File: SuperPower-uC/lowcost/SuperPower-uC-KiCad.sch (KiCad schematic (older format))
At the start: 0 parts

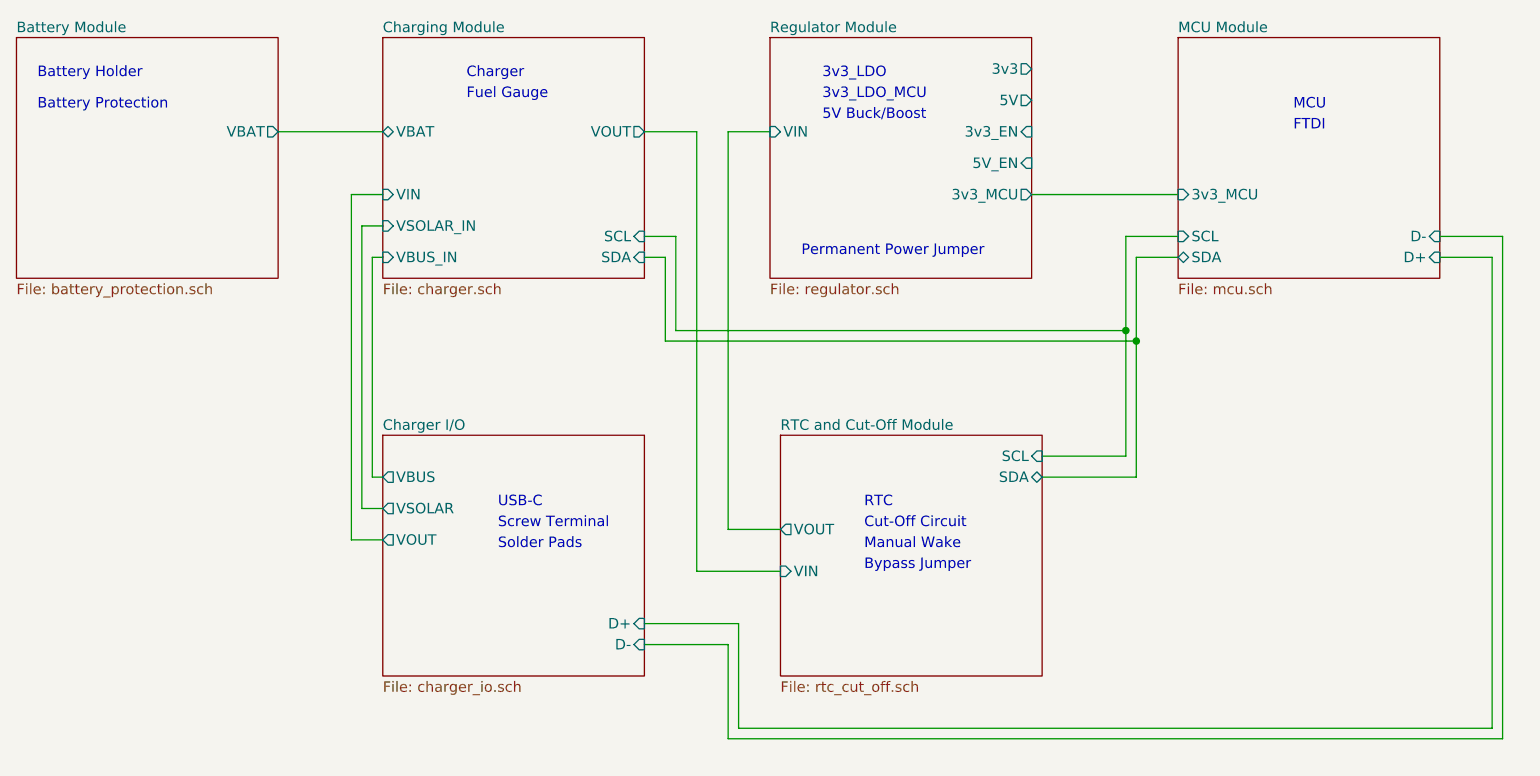
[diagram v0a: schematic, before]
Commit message: int pins and charging module
added Interrupt pins to the main sheet and finished the charging module sub sheet (with charger, fuel Gauge and power on int)
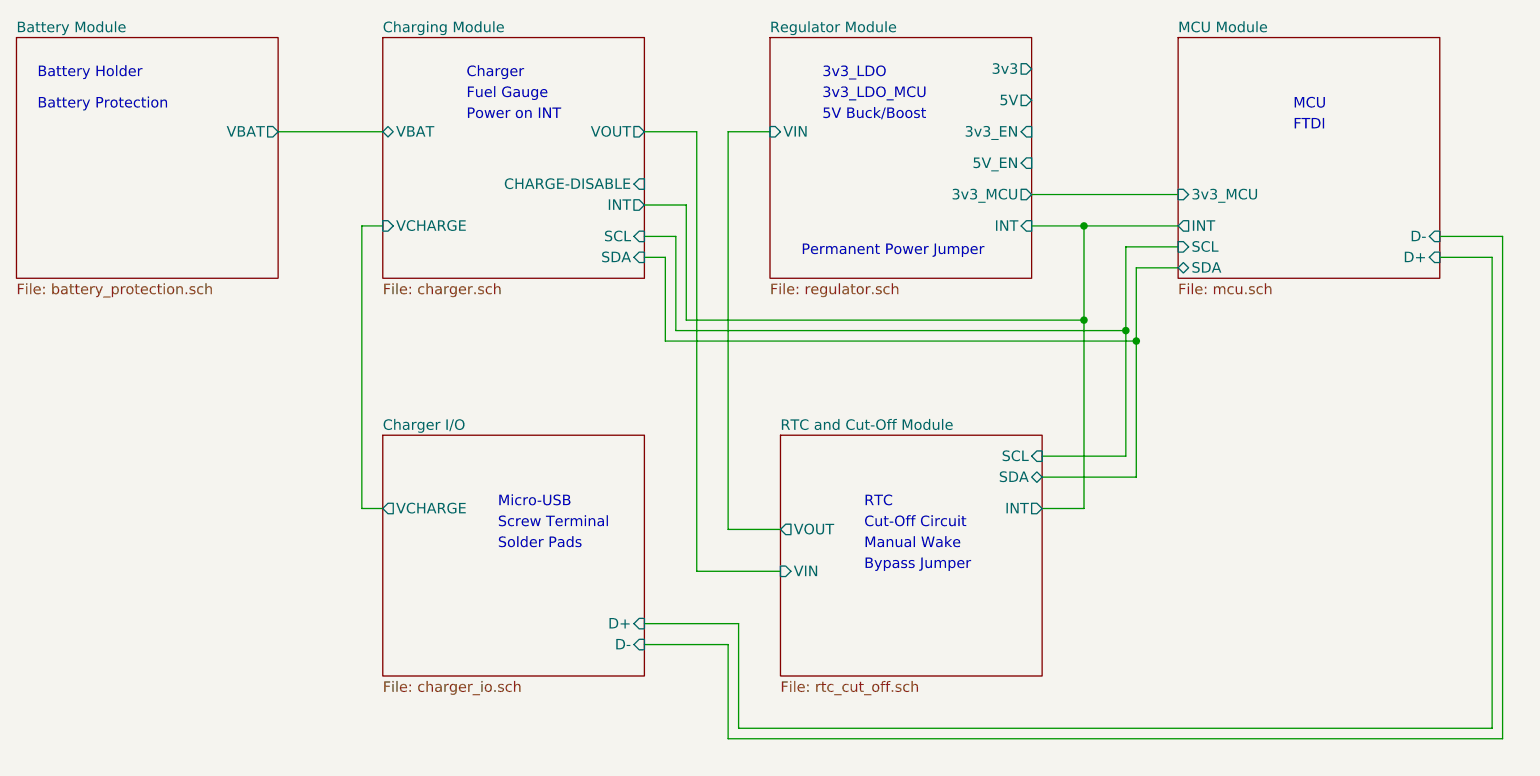
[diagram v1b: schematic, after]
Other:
- note added: "Micro-USB"
- note added: "Power on INT"
- note removed: "USB-C"
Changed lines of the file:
@@
 F0 "Charging Module" 50
 F1 "charger.sch" 50
-F2 "VBUS_IN" I L 3050 3150 50
-F3 "VIN" I L 3050 2850 50
-F4 "VSOLAR_IN" I L 3050 3000 50
-F5 "VOUT" O R 4300 2550 50
-F6 "VBAT" B L 3050 2550 50
-F7 "SCL" I R 4300 3050 50
-F8 "SDA" I R 4300 3150 50
+F2 "VOUT" O R 4300 2550 50
+F3 "VBAT" B L 3050 2550 50
+F4 "SCL" I R 4300 3050 50
+F5 "SDA" I R 4300 3150 50
+F6 "INT" O R 4300 2900 50
+F7 "VCHARGE" I L 3050 3000 50
+F8 "CHARGE-DISABLE" I R 4300 2800 50
 $EndSheet
 $Sheet
@@
 F4 "VIN" I L 4950 4650 50
 F5 "VOUT" O L 4950 4450 50
+F6 "INT" O R 6200 4350 50
 $EndSheet
 $Sheet
@@
 F6 "5V_EN" I R 6150 2700 50
 F7 "3v3_MCU" O R 6150 2850 50
+F8 "INT" I R 6150 3000 50
 $EndSheet
 $Sheet
@@
 F1 "mcu.sch" 50
 F2 "3v3_MCU" I L 6850 2850 50
-F3 "SDA" B L 6850 3150 50
-F4 "SCL" I L 6850 3050 50
+F3 "SDA" B L 6850 3200 50
+F4 "SCL" I L 6850 3100 50
 F5 "D+" I R 8100 3150 50
 F6 "D-" I R 8100 3050 50
+F7 "INT" O L 6850 3000 50
 $EndSheet
-$Sheet
-S 3050 4000 1250 1150
-U 5F63B107
-F0 "Charger I/O" 50
-F1 "charger_io.sch" 50
-F2 "VBUS" O L 3050 4200 50
-F3 "VSOLAR" O L 3050 4350 50
-F4 "VOUT" O L 3050 4500 50
-F5 "D+" I R 4300 4900 50
-F6 "D-" I R 4300 5000 50
-$EndSheet
-Wire Wire Line
-	3050 3150 3000 3150
-Wire Wire Line
-	3000 3150 3000 4200
-Wire Wire Line
-	3000 4200 3050 4200
 Wire Wire Line
 	3050 4350 2950 4350
@@
 	2950 3000 3050 3000
 Wire Wire Line
-	3050 2850 2900 2850
-Wire Wire Line
-	2900 2850 2900 4500
-Wire Wire Line
-	2900 4500 3050 4500
-Wire Wire Line
 	2550 2550 3050 2550
 Wire Wire Line
 	6850 2850 6150 2850
 Wire Wire Line
-	6850 3150 6650 3150
-Wire Wire Line
-	6650 3150 6650 3550
+	6850 3200 6650 3200
 Wire Wire Line
 	6650 4200 6200 4200
 Wire Wire Line
-	6850 3050 6600 3050
-Wire Wire Line
-	6600 3050 6600 3500
+	6850 3100 6600 3100
 Wire Wire Line
 	6600 4100 6200 4100
@@
 Cut-Off Circuit
 Text Notes 3600 4350 0    50   ~ 0
-USB-C
+Micro-USB
 Text Notes 3600 4450 0    50   ~ 0
 Screw Terminal
@@
 Text Notes 5350 4650 0    50   ~ 0
 Bypass Jumper
+Wire Wire Line
+	6650 3200 6650 3550
+Wire Wire Line
+	6600 3100 6600 3500
+Wire Wire Line
+	6850 3000 6400 3000
+Wire Wire Line
+	6200 4350 6400 4350
+Wire Wire Line
+	6400 4350 6400 3450
+Connection ~ 6400 3000
+Wire Wire Line
+	6400 3000 6150 3000
+Wire Wire Line
+	4300 2900 4500 2900
+Wire Wire Line
+	4500 2900 4500 3450
+Wire Wire Line
+	4500 3450 6400 3450
+Connection ~ 6400 3450
+Wire Wire Line
+	6400 3450 6400 3000
+$Sheet
+S 3050 4000 1250 1150
+U 5F63B107
+F0 "Charger I/O" 50
+F1 "charger_io.sch" 50
+F2 "D+" I R 4300 4900 50
+F3 "D-" I R 4300 5000 50
+F4 "VCHARGE" O L 3050 4350 50
+$EndSheet
+Text Notes 3450 2500 0    50   ~ 0
+Power on INT
 $EndSCHEMATC

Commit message: relocated ftdi to connector sheet
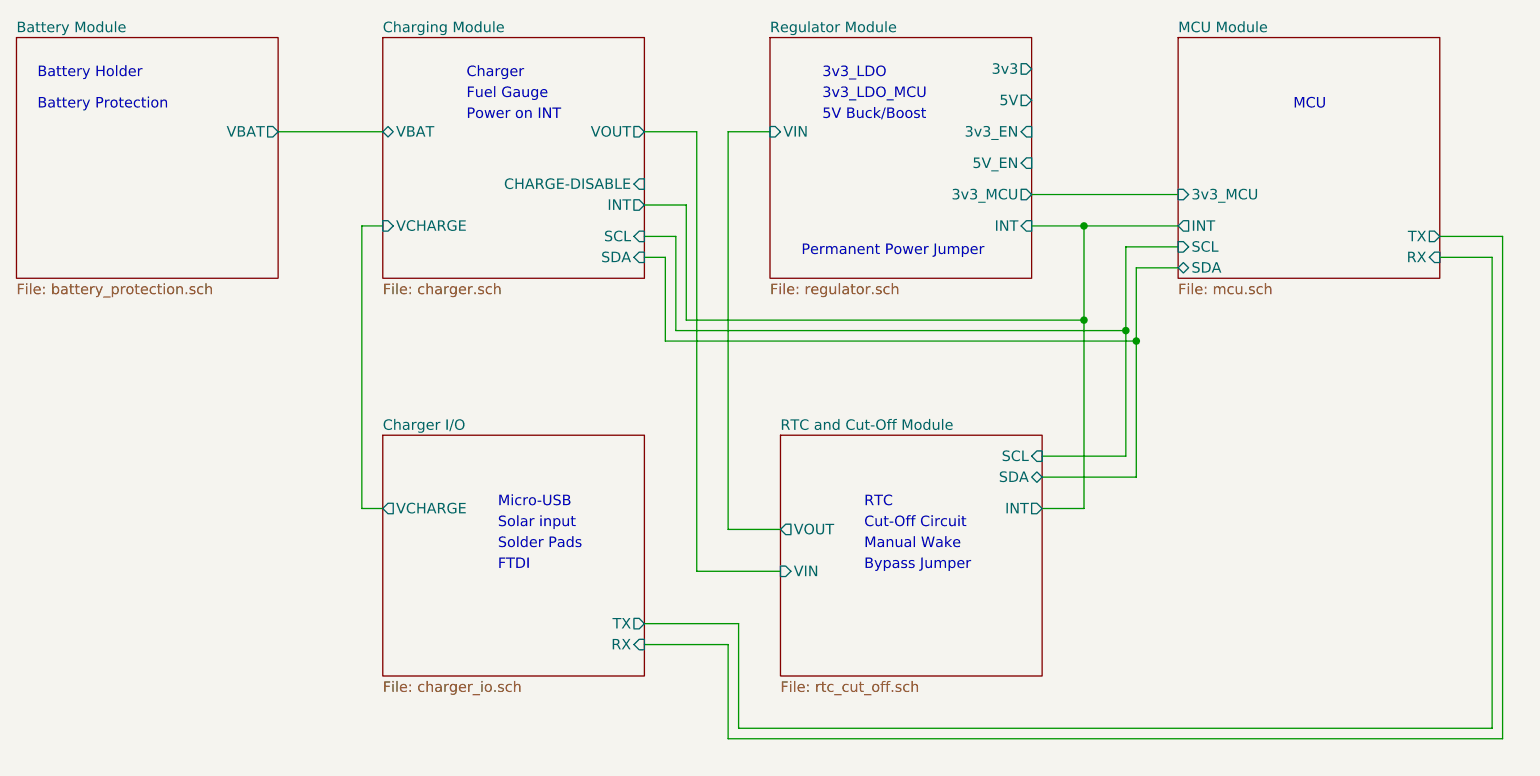
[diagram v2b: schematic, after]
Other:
- note added: "Solar input"
- note removed: "Screw Terminal"
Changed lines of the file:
@@
 F3 "SDA" B L 6850 3200 50
 F4 "SCL" I L 6850 3100 50
-F5 "D+" I R 8100 3150 50
-F6 "D-" I R 8100 3050 50
-F7 "INT" O L 6850 3000 50
+F5 "INT" O L 6850 3000 50
+F6 "TX" O R 8100 3050 50
+F7 "RX" I R 8100 3150 50
 $EndSheet
 Wire Wire Line
@@
 Micro-USB
 Text Notes 3600 4450 0    50   ~ 0
-Screw Terminal
+Solar input
 Text Notes 3600 4550 0    50   ~ 0
 Solder Pads
@@
 Text Notes 5050 3150 0    50   ~ 0
 Permanent Power Jumper
-Text Notes 7400 2550 0    50   ~ 0
-FTDI
 Text Notes 5350 4650 0    50   ~ 0
 Bypass Jumper
@@
 F0 "Charger I/O" 50
 F1 "charger_io.sch" 50
-F2 "D+" I R 4300 4900 50
-F3 "D-" I R 4300 5000 50
-F4 "VCHARGE" O L 3050 4350 50
+F2 "VCHARGE" O L 3050 4350 50
+F3 "TX" O R 4300 4900 50
+F4 "RX" I R 4300 5000 50
 $EndSheet
 Text Notes 3450 2500 0    50   ~ 0
 Power on INT
+Text Notes 3600 4650 0    50   ~ 0
+FTDI
 $EndSCHEMATC

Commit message: added ftdi and some cleanup
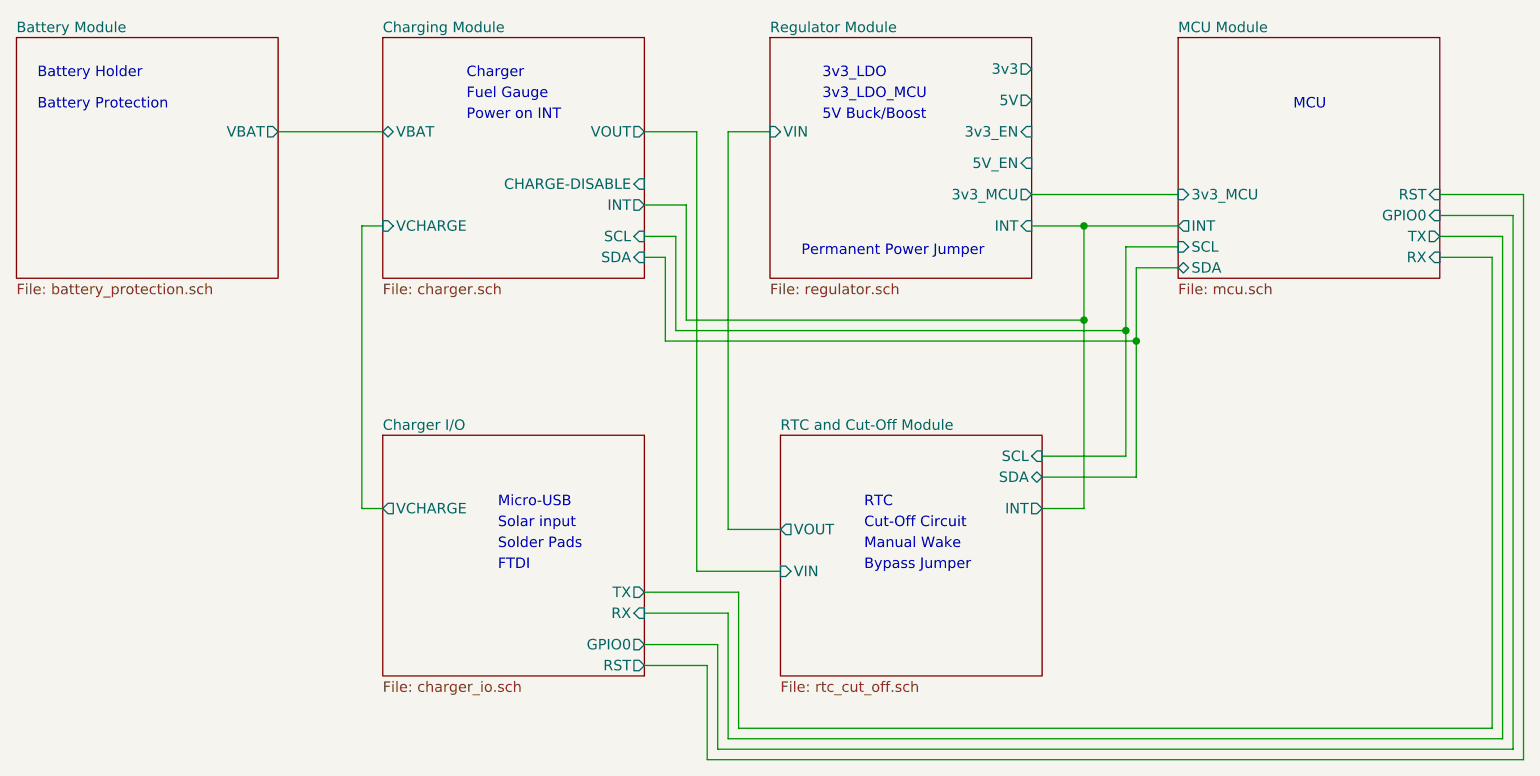
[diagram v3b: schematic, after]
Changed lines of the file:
@@
 F6 "TX" O R 8100 3050 50
 F7 "RX" I R 8100 3150 50
+F8 "RST" I R 8100 2850 50
+F9 "GPIO0" I R 8100 2950 50
 $EndSheet
 Wire Wire Line
@@
 	8350 5400 4750 5400
 Wire Wire Line
-	4750 5400 4750 4900
-Wire Wire Line
-	4750 4900 4300 4900
-Wire Wire Line
 	8350 3150 8350 5400
 Wire Wire Line
@@
 Wire Wire Line
 	8400 5450 4700 5450
-Wire Wire Line
-	4700 5450 4700 5000
-Wire Wire Line
-	4700 5000 4300 5000
 Text Notes 5050 3150 0    50   ~ 0
 Permanent Power Jumper
@@
 F1 "charger_io.sch" 50
 F2 "VCHARGE" O L 3050 4350 50
-F3 "TX" O R 4300 4900 50
-F4 "RX" I R 4300 5000 50
+F3 "TX" O R 4300 4750 50
+F4 "RX" I R 4300 4850 50
+F5 "RST" O R 4300 5100 50
+F6 "GPIO0" O R 4300 5000 50
 $EndSheet
 Text Notes 3450 2500 0    50   ~ 0
@@
 Text Notes 3600 4650 0    50   ~ 0
 FTDI
+Wire Wire Line
+	4750 4750 4300 4750
+Wire Wire Line
+	4750 4750 4750 5400
+Wire Wire Line
+	4300 4850 4700 4850
+Wire Wire Line
+	4700 4850 4700 5450
+Wire Wire Line
+	8100 2950 8450 2950
+Wire Wire Line
+	8450 2950 8450 5500
+Wire Wire Line
+	8450 5500 4650 5500
+Wire Wire Line
+	4650 5500 4650 5000
+Wire Wire Line
+	4650 5000 4300 5000
+Wire Wire Line
+	4300 5100 4600 5100
+Wire Wire Line
+	4600 5100 4600 5550
+Wire Wire Line
+	4600 5550 8500 5550
+Wire Wire Line
+	8500 5550 8500 2850
+Wire Wire Line
+	8500 2850 8100 2850
 $EndSCHEMATC

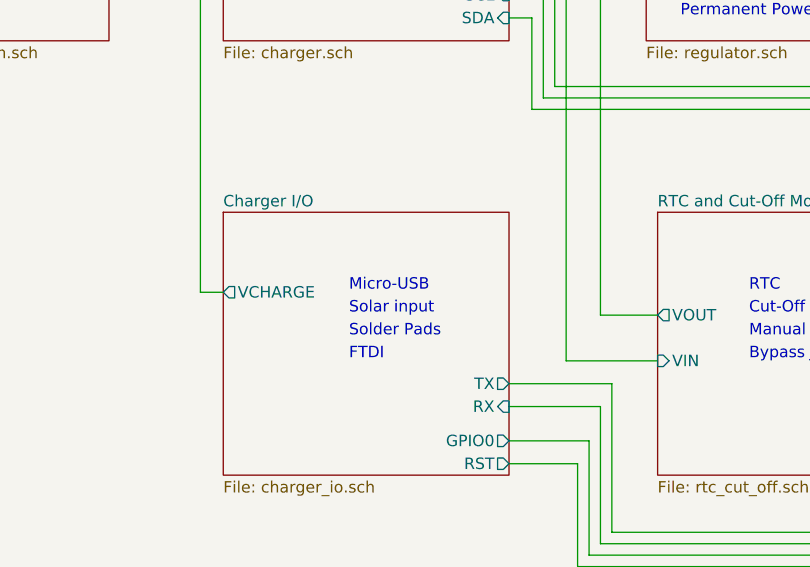
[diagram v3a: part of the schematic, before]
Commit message: fixed mentioned issues and swapped micro usb with usb c
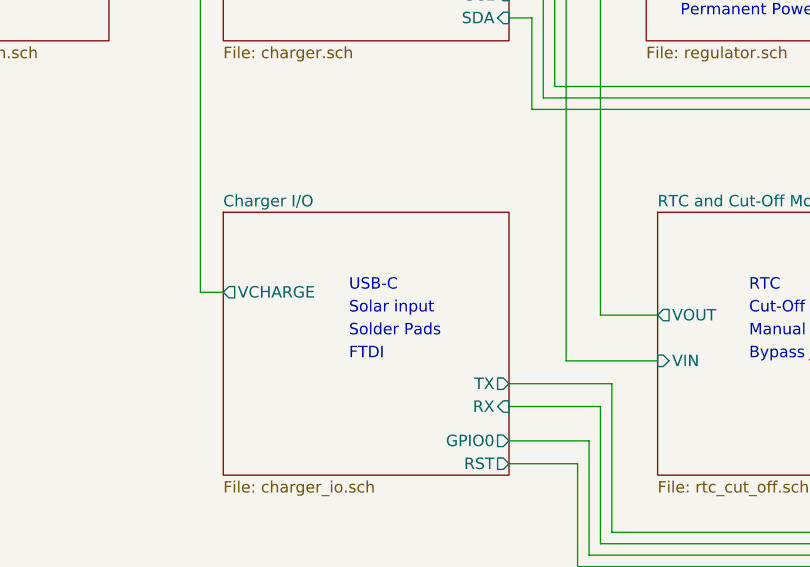
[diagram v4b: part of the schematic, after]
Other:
- note added: "USB-C"
- note removed: "Micro-USB"
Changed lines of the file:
@@
 Cut-Off Circuit
 Text Notes 3600 4350 0    50   ~ 0
-Micro-USB
+USB-C
 Text Notes 3600 4450 0    50   ~ 0
 Solar input

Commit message: io expander, rtc cirquit, i2c pullup...
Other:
- note added: "I2C pullup"
- note added: "IO Expander"
- note removed: "Cut-Off Circuit"
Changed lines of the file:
@@
 F0 "Battery Module" 50
 F1 "battery_protection.sch" 50
-F2 "VBAT" O R 2550 2550 50
+F2 "VBAT" B R 2550 2550 50
 $EndSheet
 $Sheet
@@
 F0 "Charging Module" 50
 F1 "charger.sch" 50
-F2 "VOUT" O R 4300 2550 50
-F3 "VBAT" B L 3050 2550 50
-F4 "SCL" I R 4300 3050 50
-F5 "SDA" I R 4300 3150 50
-F6 "INT" O R 4300 2900 50
-F7 "VCHARGE" I L 3050 3000 50
-F8 "CHARGE-DISABLE" I R 4300 2800 50
+F2 "SCL" I R 4300 3050 50
+F3 "SDA" I R 4300 3150 50
+F4 "INT" O R 4300 2900 50
+F5 "VCHARGE" I L 3050 3000 50
+F6 "CHARGE-DISABLE" I R 4300 2800 50
+F7 "VBAT" B L 3050 2550 50
 $EndSheet
 $Sheet
@@
 F2 "SCL" I R 6200 4100 50
 F3 "SDA" B R 6200 4200 50
-F4 "VIN" I L 4950 4650 50
-F5 "VOUT" O L 4950 4450 50
-F6 "INT" O R 6200 4350 50
+F4 "INT" O R 6200 4350 50
+F5 "VBAT" I L 4950 4450 50
+F6 "3.3V_EN" O R 6200 4600 50
+F7 "5V_EN" O R 6200 4500 50
 $EndSheet
 $Sheet
@@
 F0 "Regulator Module" 50
 F1 "regulator.sch" 50
-F2 "VIN" I L 4900 2550 50
-F3 "3v3" O R 6150 2250 50
-F4 "5V" O R 6150 2400 50
-F5 "3v3_EN" I R 6150 2550 50
-F6 "5V_EN" I R 6150 2700 50
-F7 "3v3_MCU" O R 6150 2850 50
-F8 "INT" I R 6150 3000 50
+F2 "3v3" O R 6150 2250 50
+F3 "5V" O R 6150 2400 50
+F4 "3v3_EN" I R 6150 2550 50
+F5 "5V_EN" I R 6150 2700 50
+F6 "3v3_MCU" O R 6150 2850 50
+F7 "INT" I R 6150 3000 50
+F8 "VBAT" I L 4900 2550 50
 $EndSheet
 $Sheet
@@
 	2950 3000 3050 3000
 Wire Wire Line
-	2550 2550 3050 2550
+	2550 2550 2900 2550
 Wire Wire Line
 	6850 2850 6150 2850
@@
 	6600 4100 6200 4100
 Wire Wire Line
-	4300 2550 4550 2550
-Wire Wire Line
-	4550 2550 4550 4650
-Wire Wire Line
-	4550 4650 4950 4650
-Wire Wire Line
 	4950 4450 4700 4450
 Wire Wire Line
-	4700 4450 4700 2550
+	4700 4450 4700 3600
 Wire Wire Line
 	4700 2550 4900 2550
@@
 Text Notes 7400 2450 0    50   ~ 0
 MCU
-Text Notes 5350 4350 0    50   ~ 0
+Text Notes 5300 4350 0    50   ~ 0
 RTC
-Text Notes 5350 4450 0    50   ~ 0
-Cut-Off Circuit
 Text Notes 3600 4350 0    50   ~ 0
 USB-C
@@
 Wire Wire Line
 	6650 3550 6650 4200
-Text Notes 5350 4550 0    50   ~ 0
+Text Notes 5300 4550 0    50   ~ 0
 Manual Wake
 Wire Wire Line
@@
 Text Notes 5050 3150 0    50   ~ 0
 Permanent Power Jumper
-Text Notes 5350 4650 0    50   ~ 0
+Text Notes 5300 4650 0    50   ~ 0
 Bypass Jumper
 Wire Wire Line
@@
 Wire Wire Line
 	8500 2850 8100 2850
+Wire Wire Line
+	4700 3600 2900 3600
+Wire Wire Line
+	2900 3600 2900 2550
+Connection ~ 4700 3600
+Wire Wire Line
+	4700 3600 4700 2550
+Connection ~ 2900 2550
+Wire Wire Line
+	2900 2550 3050 2550
+Text Notes 5300 4450 0    50   ~ 0
+IO Expander
+Text Notes 5300 4750 0    50   ~ 0
+I2C pullup
+Wire Wire Line
+	6500 4600 6500 2550
+Wire Wire Line
+	6200 4600 6500 4600
+Wire Wire Line
+	6150 2550 6500 2550
+Wire Wire Line
+	6150 2700 6450 2700
+Wire Wire Line
+	6450 2700 6450 4500
+Wire Wire Line
+	6450 4500 6200 4500
 $EndSCHEMATC

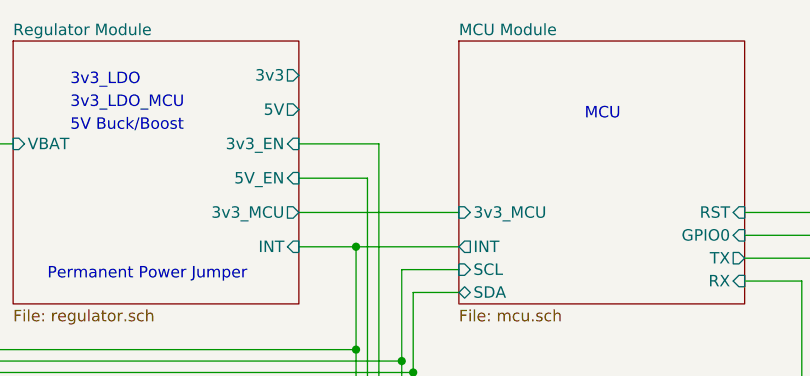
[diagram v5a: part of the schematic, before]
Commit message: naming fixes, more components and continued schematics
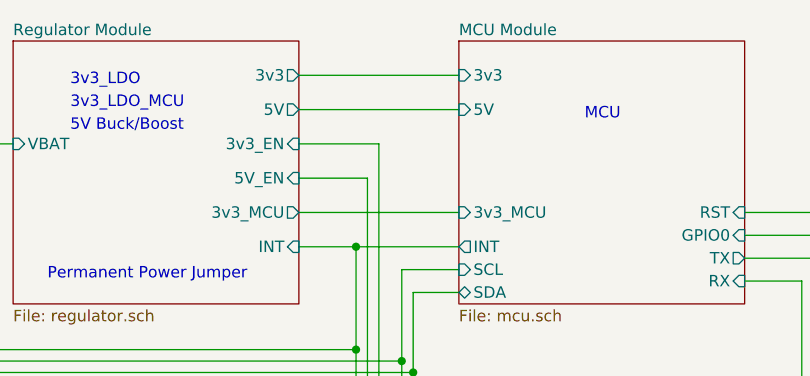
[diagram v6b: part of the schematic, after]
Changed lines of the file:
@@
 F8 "RST" I R 8100 2850 50
 F9 "GPIO0" I R 8100 2950 50
+F10 "3v3" I L 6850 2250 50
+F11 "5V" I L 6850 2400 50
 $EndSheet
 Wire Wire Line
@@
 Wire Wire Line
 	6450 4500 6200 4500
+Wire Wire Line
+	6850 2250 6150 2250
+Wire Wire Line
+	6150 2400 6850 2400
 $EndSCHEMATC

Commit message: schematic layout cleaning
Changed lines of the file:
@@
 F3 "SDA" B L 6850 3200 50
 F4 "SCL" I L 6850 3100 50
-F5 "INT" O L 6850 3000 50
-F6 "TX" O R 8100 3050 50
-F7 "RX" I R 8100 3150 50
-F8 "RST" I R 8100 2850 50
-F9 "GPIO0" I R 8100 2950 50
-F10 "3v3" I L 6850 2250 50
-F11 "5V" I L 6850 2400 50
+F5 "TX" O R 8100 3050 50
+F6 "RX" I R 8100 3150 50
+F7 "RST" I R 8100 2850 50
+F8 "GPIO0" I R 8100 2950 50
+F9 "3v3" I L 6850 2250 50
+F10 "5V" I L 6850 2400 50
 $EndSheet
 Wire Wire Line
@@
 	6600 3100 6600 3500
 Wire Wire Line
-	6850 3000 6400 3000
-Wire Wire Line
 	6200 4350 6400 4350
 Wire Wire Line
 	6400 4350 6400 3450
-Connection ~ 6400 3000
 Wire Wire Line
 	6400 3000 6150 3000
